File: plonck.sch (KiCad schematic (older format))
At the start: 127 parts, among them J1 Battery_connector, J2 SWD, Q1 Q_PMOS_GSD, SW1 SW_Push, U1 SRV05-4, U2 TP4054-42-SOT25-R, U3 XC6206PxxxMR-Regulator_Linear, U4 nRF52840_holyiot_18010, q1 USB4085-GF-A_REVA

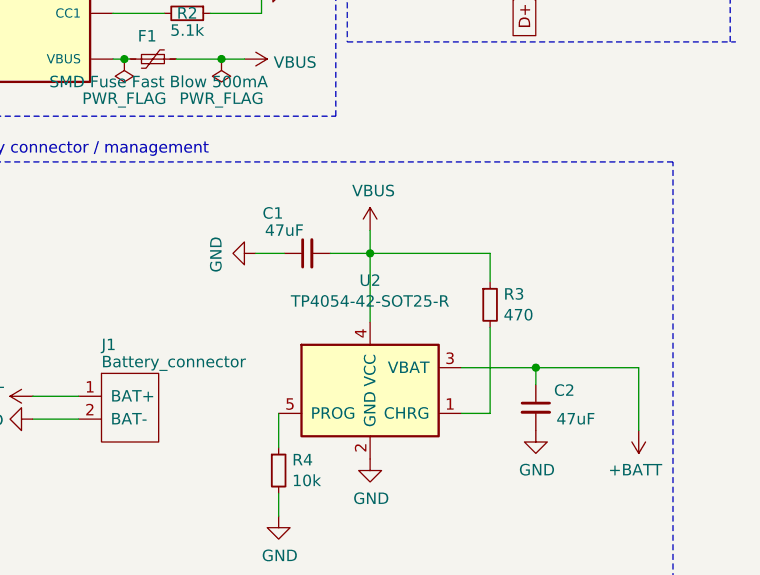
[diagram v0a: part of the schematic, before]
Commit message: added charge status led
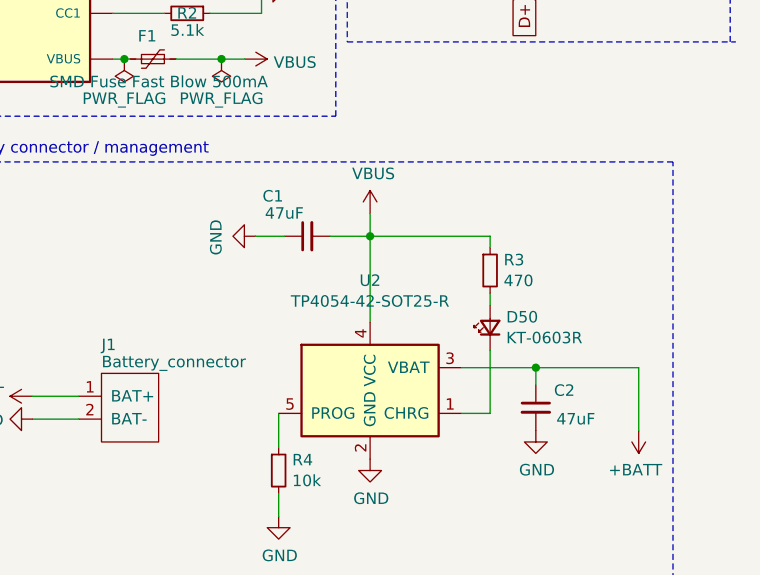
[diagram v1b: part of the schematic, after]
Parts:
- added D50: KT-0603R, LED_SMD:LED_0603_1608Metric, symbol Device:LED_Small
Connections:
- net at R3.2: now also D50.2 (A); no longer U2.1 (CHRG)
- new net: D50.1 (K), U2.1 (CHRG)
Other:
- moved on the sheet: C1, R3
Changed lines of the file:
@@
 L Device:C_Small C1
 U 1 1 60625507
-P 8775 3075
-F 0 "C1" V 8950 3225 50  0000 C CNN
-F 1 "47uF" V 8875 3175 50  0000 C CNN
-F 2 "Capacitor_SMD:C_1206_3216Metric" H 8775 3075 50  0001 C CNN
-F 3 "~" H 8775 3075 50  0001 C CNN
-F 4 "C96123" H 8775 3075 50  0001 C CNN "LCSC"
-	1    8775 3075
+P 8775 3000
+F 0 "C1" V 8950 3150 50  0000 C CNN
+F 1 "47uF" V 8875 3100 50  0000 C CNN
+F 2 "Capacitor_SMD:C_1206_3216Metric" H 8775 3000 50  0001 C CNN
+F 3 "~" H 8775 3000 50  0001 C CNN
+F 4 "C96123" H 8775 3000 50  0001 C CNN "LCSC"
+	1    8775 3000
 	0    -1   -1   0
 $EndComp
 Wire Wire Line
-	9050 2975 9050 3075
-Wire Wire Line
-	8875 3075 9050 3075
-Wire Wire Line
-	8550 3075 8675 3075
+	9050 2900 9050 3000
+Wire Wire Line
+	8875 3000 9050 3000
+Wire Wire Line
+	8550 3000 8675 3000
 $Comp
 L power:GND #PWR07
 U 1 1 6063374E
-P 8550 3075
-F 0 "#PWR07" H 8550 2825 50  0001 C CNN
-F 1 "GND" H 8555 2902 50  0000 C CNN
-F 2 "" H 8550 3075 50  0001 C CNN
-F 3 "" H 8550 3075 50  0001 C CNN
-	1    8550 3075
+P 8550 3000
+F 0 "#PWR07" H 8550 2750 50  0001 C CNN
+F 1 "GND" H 8555 2827 50  0000 C CNN
+F 2 "" H 8550 3000 50  0001 C CNN
+F 3 "" H 8550 3000 50  0001 C CNN
+	1    8550 3000
 	0    1    1    0
 $EndComp
-Connection ~ 9050 3075
-Wire Wire Line
-	9050 3075 9050 3375
-Wire Wire Line
-	9050 3075 9575 3075
-Wire Wire Line
-	9575 3075 9575 3200
-Wire Wire Line
-	9575 3775 9575 3400
+Connection ~ 9050 3000
+Wire Wire Line
+	9050 3000 9050 3375
+Wire Wire Line
+	9050 3000 9575 3000
+Wire Wire Line
+	9575 3000 9575 3050
+Wire Wire Line
+	9575 3775 9575 3500
 Wire Wire Line
 	9575 3775 9450 3775
@@
 L power:VBUS #PWR06
 U 1 1 607C3C76
-P 9050 2975
-F 0 "#PWR06" H 9050 2825 50  0001 C CNN
-F 1 "VBUS" H 9065 3148 50  0000 C CNN
-F 2 "" H 9050 2975 50  0001 C CNN
-F 3 "" H 9050 2975 50  0001 C CNN
-	1    9050 2975
+P 9050 2900
+F 0 "#PWR06" H 9050 2750 50  0001 C CNN
+F 1 "VBUS" H 9065 3073 50  0000 C CNN
+F 2 "" H 9050 2900 50  0001 C CNN
+F 3 "" H 9050 2900 50  0001 C CNN
+	1    9050 2900
 	1    0    0    -1
 $EndComp
@@
 L Device:R_Small R3
 U 1 1 6063443F
-P 9575 3300
-F 0 "R3" H 9634 3346 50  0000 L CNN
-F 1 "470" H 9634 3255 50  0000 L CNN
-F 2 "Resistor_SMD:R_0603_1608Metric" H 9575 3300 50  0001 C CNN
-F 3 "~" H 9575 3300 50  0001 C CNN
-F 4 "RMCF0603JT470RTR-ND" H 9575 3300 50  0001 C CNN "Digikey"
-F 5 "C23179" H 9575 3300 50  0001 C CNN "LCSC"
-	1    9575 3300
+P 9575 3150
+F 0 "R3" H 9634 3196 50  0000 L CNN
+F 1 "470" H 9634 3105 50  0000 L CNN
+F 2 "Resistor_SMD:R_0603_1608Metric" H 9575 3150 50  0001 C CNN
+F 3 "~" H 9575 3150 50  0001 C CNN
+F 4 "RMCF0603JT470RTR-ND" H 9575 3150 50  0001 C CNN "Digikey"
+F 5 "C23179" H 9575 3150 50  0001 C CNN "LCSC"
+	1    9575 3150
 	1    0    0    -1
 $EndComp
@@
 Wire Notes Line
 	2375 6550 3325 6550
+$Comp
+L Device:LED_Small D50
+U 1 1 60BDAFE9
+P 9575 3400
+F 0 "D50" V 9621 3330 50  0000 R CNN
+F 1 "KT-0603R" V 9530 3330 50  0000 R CNN
+F 2 "LED_SMD:LED_0603_1608Metric" V 9575 3400 50  0001 C CNN
+F 3 "https://datasheet.lcsc.com/szlcsc/Hubei-KENTO-Elec-KT-0603R_C2286.pdf" V 9575 3400 50  0001 C CNN
+F 4 "C2286" H 9575 3400 50  0001 C CNN "LCSC"
+	1    9575 3400
+	0    -1   -1   0
+$EndComp
+Wire Wire Line
+	9575 3300 9575 3250
 $EndSCHEMATC

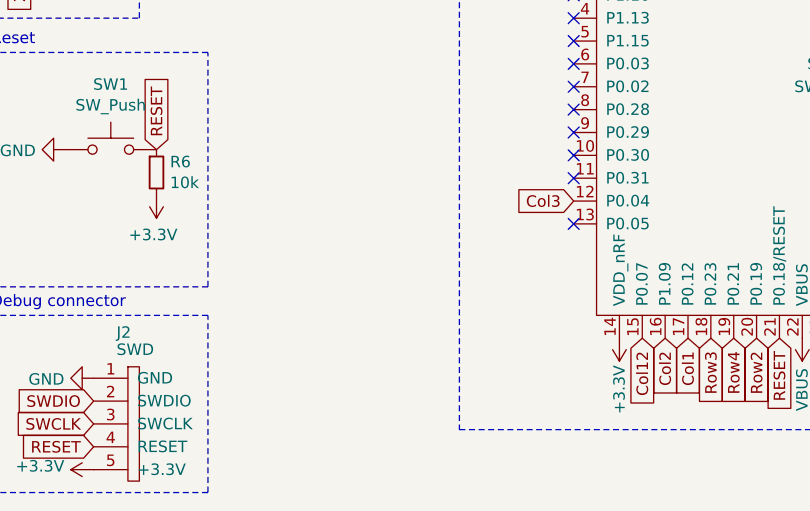
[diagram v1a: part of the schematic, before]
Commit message: added vsense circuitry
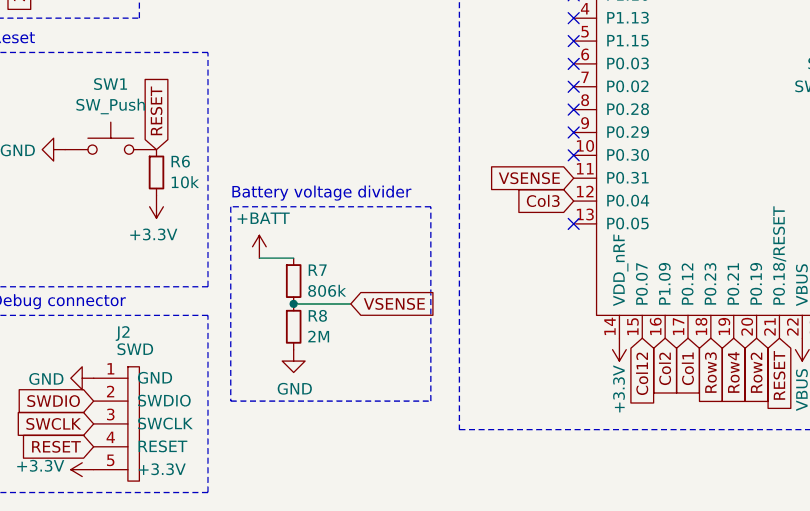
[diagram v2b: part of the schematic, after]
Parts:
- added R7: 806k, Resistor_SMD:R_0603_1608Metric, symbol Device:R_Small
- added R8: 2M, Resistor_SMD:R_0603_1608Metric, symbol Device:R_Small
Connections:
- net +BATT: now also R7.1
- net GND: now also R8.2
- net VSENSE: now reaches U4.11 (P0.31)
- net VSENSE: now also R7.2, R8.1
- no-connect marks 15 -> 14
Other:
- note added: "Battery voltage divider"
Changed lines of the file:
@@
 Col3
 NoConn ~ 4925 6275
-NoConn ~ 4925 6075
 NoConn ~ 4925 5975
 NoConn ~ 4925 5875
@@
 Wire Wire Line
 	9575 3300 9575 3250
+$Comp
+L power:+BATT #PWR0101
+U 1 1 60C1F4E5
+P 3550 6425
+F 0 "#PWR0101" H 3550 6275 50  0001 C CNN
+F 1 "+BATT" H 3565 6598 50  0000 C CNN
+F 2 "" H 3550 6425 50  0001 C CNN
+F 3 "" H 3550 6425 50  0001 C CNN
+	1    3550 6425
+	1    0    0    -1
+$EndComp
+$Comp
+L Device:R_Small R7
+U 1 1 60C2226C
+P 3700 6525
+F 0 "R7" H 3759 6571 50  0000 L CNN
+F 1 "806k" H 3759 6480 50  0000 L CNN
+F 2 "Resistor_SMD:R_0603_1608Metric" H 3700 6525 50  0001 C CNN
+F 3 "~" H 3700 6525 50  0001 C CNN
+	1    3700 6525
+	1    0    0    -1
+$EndComp
+$Comp
+L Device:R_Small R8
+U 1 1 60C23717
+P 3700 6725
+F 0 "R8" H 3759 6771 50  0000 L CNN
+F 1 "2M" H 3759 6680 50  0000 L CNN
+F 2 "Resistor_SMD:R_0603_1608Metric" H 3700 6725 50  0001 C CNN
+F 3 "~" H 3700 6725 50  0001 C CNN
+	1    3700 6725
+	1    0    0    -1
+$EndComp
+$Comp
+L power:GND #PWR0102
+U 1 1 60C25DD1
+P 3700 6825
+F 0 "#PWR0102" H 3700 6575 50  0001 C CNN
+F 1 "GND" H 3705 6652 50  0000 C CNN
+F 2 "" H 3700 6825 50  0001 C CNN
+F 3 "" H 3700 6825 50  0001 C CNN
+	1    3700 6825
+	1    0    0    -1
+$EndComp
+Wire Wire Line
+	3550 6425 3700 6425
+Wire Wire Line
+	3700 6625 3950 6625
+Connection ~ 3700 6625
+Text GLabel 3950 6625 2    50   Input ~ 0
+VSENSE
+Wire Notes Line
+	3425 6200 3425 7050
+Wire Notes Line
+	3425 7050 4300 7050
+Wire Notes Line
+	4300 7050 4300 6200
+Wire Notes Line
+	4300 6200 3425 6200
+Text Notes 3425 6175 0    50   ~ 0
+Battery voltage divider
+Text GLabel 4925 6075 0    50   Input ~ 0
+VSENSE
 $EndSCHEMATC

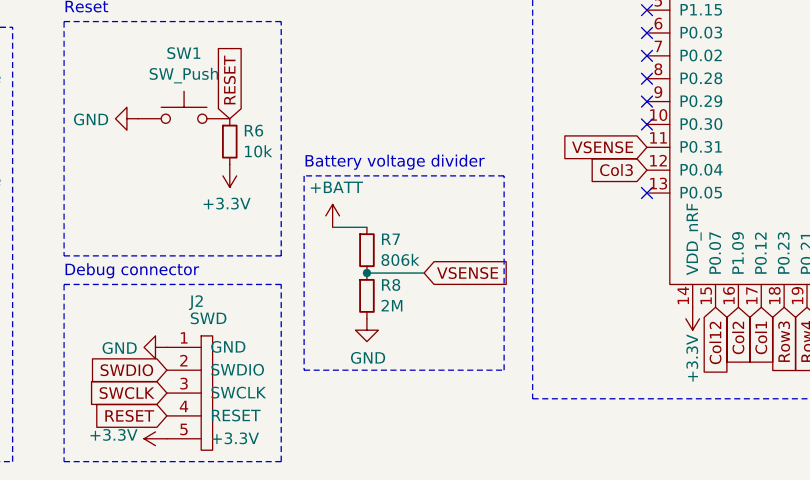
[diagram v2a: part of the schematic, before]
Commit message: updated resistor values in battery voltage divider
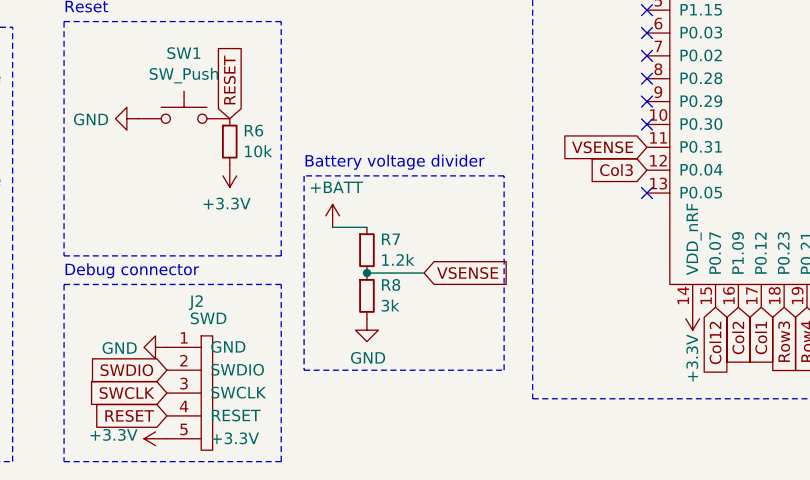
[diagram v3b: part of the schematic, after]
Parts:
- R7: value 806k -> 1.2k; LCSC (none) -> C22765
- R8: value 2M -> 3k; LCSC (none) -> C17661
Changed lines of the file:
@@
 P 3700 6525
 F 0 "R7" H 3759 6571 50  0000 L CNN
-F 1 "806k" H 3759 6480 50  0000 L CNN
+F 1 "1.2k" H 3759 6480 50  0000 L CNN
 F 2 "Resistor_SMD:R_0603_1608Metric" H 3700 6525 50  0001 C CNN
-F 3 "~" H 3700 6525 50  0001 C CNN
+F 3 "https://datasheet.lcsc.com/lcsc/1811021221_UNI-ROYAL-Uniroyal-Elec-0603WAF1201T5E_C22765.pdf" H 3700 6525 50  0001 C CNN
+F 4 "C22765" H 3700 6525 50  0001 C CNN "LCSC"
 	1    3700 6525
 	1    0    0    -1
@@
 P 3700 6725
 F 0 "R8" H 3759 6771 50  0000 L CNN
-F 1 "2M" H 3759 6680 50  0000 L CNN
+F 1 "3k" H 3759 6680 50  0000 L CNN
 F 2 "Resistor_SMD:R_0603_1608Metric" H 3700 6725 50  0001 C CNN
-F 3 "~" H 3700 6725 50  0001 C CNN
+F 3 "https://datasheet.lcsc.com/lcsc/1811131122_UNI-ROYAL-Uniroyal-Elec-0805W8F3001T5E_C17661.pdf" H 3700 6725 50  0001 C CNN
+F 4 "C17661" H 3700 6725 50  0001 C CNN "LCSC"
 	1    3700 6725
 	1    0    0    -1

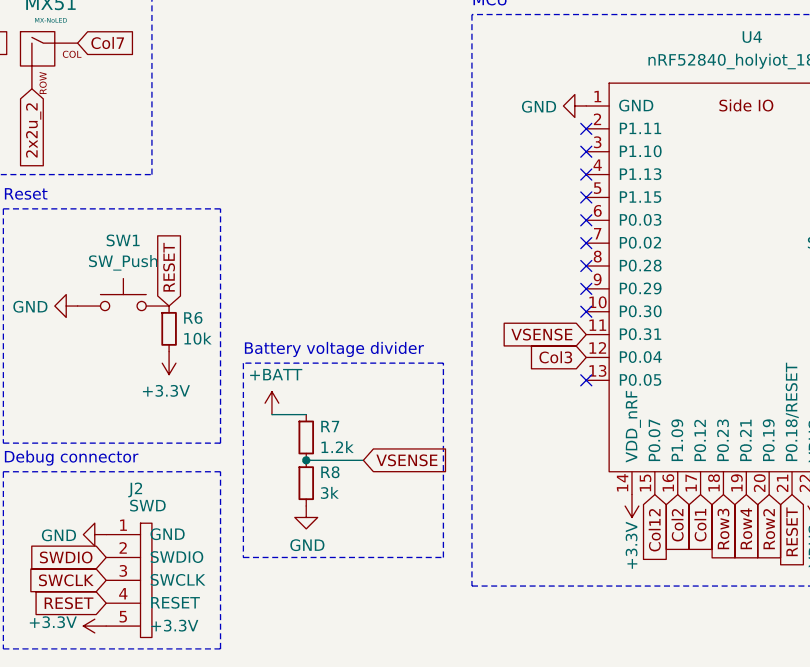
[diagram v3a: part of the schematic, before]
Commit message: added bootloader status led
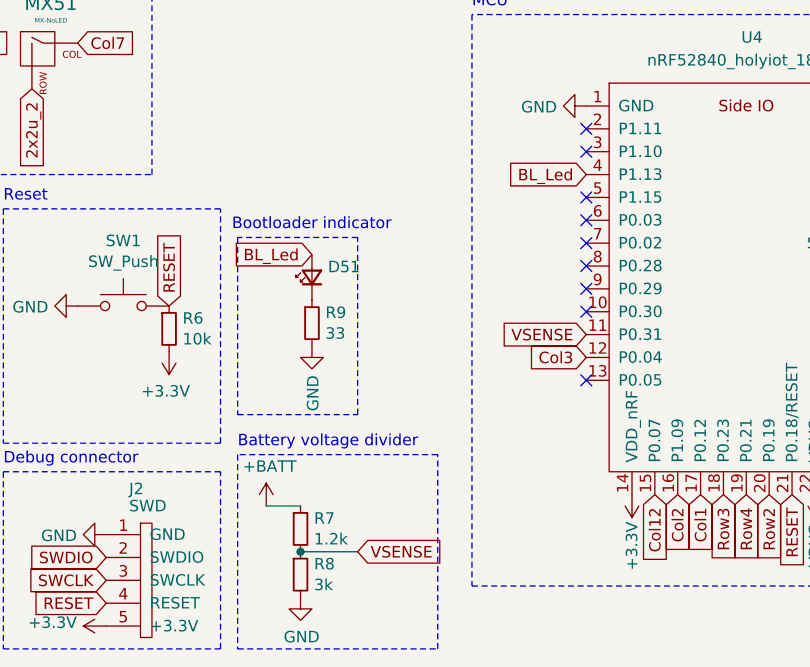
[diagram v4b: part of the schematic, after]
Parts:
- added D51: 19-217/BHC-ZL1M2RY/3T, LED_SMD:LED_0603_1608Metric, symbol Device:LED_Small
- added R9: 33, Resistor_SMD:R_0603_1608Metric, symbol Device:R_Small
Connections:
- net GND: now also R9.2
- net BL_Led: now reaches U4.4 (P1.13)
- net BL_Led: now also D51.2 (A)
- new net: D51.1 (K), R9.1
- no-connect marks 14 -> 13
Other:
- note added: "Bootloader indicator"
- moved on the sheet: R7, R8
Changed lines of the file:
@@
 NoConn ~ 4925 5575
 NoConn ~ 4925 5475
-NoConn ~ 4925 5375
 NoConn ~ 4925 5275
 NoConn ~ 4925 5175
@@
 L power:+BATT #PWR0101
 U 1 1 60C1F4E5
-P 3550 6425
-F 0 "#PWR0101" H 3550 6275 50  0001 C CNN
-F 1 "+BATT" H 3565 6598 50  0000 C CNN
-F 2 "" H 3550 6425 50  0001 C CNN
-F 3 "" H 3550 6425 50  0001 C CNN
-	1    3550 6425
+P 3525 6825
+F 0 "#PWR0101" H 3525 6675 50  0001 C CNN
+F 1 "+BATT" H 3540 6998 50  0000 C CNN
+F 2 "" H 3525 6825 50  0001 C CNN
+F 3 "" H 3525 6825 50  0001 C CNN
+	1    3525 6825
 	1    0    0    -1
 $EndComp
@@
 L Device:R_Small R7
 U 1 1 60C2226C
-P 3700 6525
-F 0 "R7" H 3759 6571 50  0000 L CNN
-F 1 "1.2k" H 3759 6480 50  0000 L CNN
-F 2 "Resistor_SMD:R_0603_1608Metric" H 3700 6525 50  0001 C CNN
-F 3 "https://datasheet.lcsc.com/lcsc/1811021221_UNI-ROYAL-Uniroyal-Elec-0603WAF1201T5E_C22765.pdf" H 3700 6525 50  0001 C CNN
-F 4 "C22765" H 3700 6525 50  0001 C CNN "LCSC"
-	1    3700 6525
+P 3675 6925
+F 0 "R7" H 3734 6971 50  0000 L CNN
+F 1 "1.2k" H 3734 6880 50  0000 L CNN
+F 2 "Resistor_SMD:R_0603_1608Metric" H 3675 6925 50  0001 C CNN
+F 3 "https://datasheet.lcsc.com/lcsc/1811021221_UNI-ROYAL-Uniroyal-Elec-0603WAF1201T5E_C22765.pdf" H 3675 6925 50  0001 C CNN
+F 4 "C22765" H 3675 6925 50  0001 C CNN "LCSC"
+	1    3675 6925
 	1    0    0    -1
 $EndComp
@@
 L Device:R_Small R8
 U 1 1 60C23717
-P 3700 6725
-F 0 "R8" H 3759 6771 50  0000 L CNN
-F 1 "3k" H 3759 6680 50  0000 L CNN
-F 2 "Resistor_SMD:R_0603_1608Metric" H 3700 6725 50  0001 C CNN
-F 3 "https://datasheet.lcsc.com/lcsc/1811131122_UNI-ROYAL-Uniroyal-Elec-0805W8F3001T5E_C17661.pdf" H 3700 6725 50  0001 C CNN
-F 4 "C17661" H 3700 6725 50  0001 C CNN "LCSC"
-	1    3700 6725
+P 3675 7125
+F 0 "R8" H 3734 7171 50  0000 L CNN
+F 1 "3k" H 3734 7080 50  0000 L CNN
+F 2 "Resistor_SMD:R_0603_1608Metric" H 3675 7125 50  0001 C CNN
+F 3 "https://datasheet.lcsc.com/lcsc/1811131122_UNI-ROYAL-Uniroyal-Elec-0805W8F3001T5E_C17661.pdf" H 3675 7125 50  0001 C CNN
+F 4 "C17661" H 3675 7125 50  0001 C CNN "LCSC"
+	1    3675 7125
 	1    0    0    -1
 $EndComp
@@
 L power:GND #PWR0102
 U 1 1 60C25DD1
-P 3700 6825
-F 0 "#PWR0102" H 3700 6575 50  0001 C CNN
-F 1 "GND" H 3705 6652 50  0000 C CNN
-F 2 "" H 3700 6825 50  0001 C CNN
-F 3 "" H 3700 6825 50  0001 C CNN
-	1    3700 6825
-	1    0    0    -1
-$EndComp
-Wire Wire Line
-	3550 6425 3700 6425
-Wire Wire Line
-	3700 6625 3950 6625
-Connection ~ 3700 6625
-Text GLabel 3950 6625 2    50   Input ~ 0
+P 3675 7225
+F 0 "#PWR0102" H 3675 6975 50  0001 C CNN
+F 1 "GND" H 3680 7052 50  0000 C CNN
+F 2 "" H 3675 7225 50  0001 C CNN
+F 3 "" H 3675 7225 50  0001 C CNN
+	1    3675 7225
+	1    0    0    -1
+$EndComp
+Wire Wire Line
+	3525 6825 3675 6825
+Wire Wire Line
+	3675 7025 3925 7025
+Connection ~ 3675 7025
+Text GLabel 3925 7025 2    50   Input ~ 0
 VSENSE
 Wire Notes Line
-	3425 6200 3425 7050
-Wire Notes Line
-	3425 7050 4300 7050
-Wire Notes Line
-	4300 7050 4300 6200
-Wire Notes Line
-	4300 6200 3425 6200
-Text Notes 3425 6175 0    50   ~ 0
+	3400 6600 3400 7450
+Wire Notes Line
+	3400 7450 4275 7450
+Wire Notes Line
+	4275 7450 4275 6600
+Wire Notes Line
+	4275 6600 3400 6600
+Text Notes 3400 6575 0    50   ~ 0
 Battery voltage divider
 Text GLabel 4925 6075 0    50   Input ~ 0
 VSENSE
+Text GLabel 3725 5725 0    50   Input ~ 0
+BL_Led
+$Comp
+L Device:LED_Small D51
+U 1 1 60BA6345
+P 3725 5825
+F 0 "D51" V 3771 5755 50  0000 R CNN
+F 1 "19-217/BHC-ZL1M2RY/3T" V 3680 5755 50  0001 R CNN
+F 2 "LED_SMD:LED_0603_1608Metric" V 3725 5825 50  0001 C CNN
+F 3 "https://datasheet.lcsc.com/lcsc/1811101510_Everlight-Elec-19-217-BHC-ZL1M2RY-3T_C72041.pdf" V 3725 5825 50  0001 C CNN
+F 4 "C72041" H 3725 5825 50  0001 C CNN "LCSC"
+	1    3725 5825
+	0    -1   -1   0
+$EndComp
+$Comp
+L power:GND #PWR035
+U 1 1 60BA897F
+P 3725 6125
+F 0 "#PWR035" H 3725 5875 50  0001 C CNN
+F 1 "GND" V 3730 5997 50  0000 R CNN
+F 2 "" H 3725 6125 50  0001 C CNN
+F 3 "" H 3725 6125 50  0001 C CNN
+	1    3725 6125
+	1    0    0    -1
+$EndComp
+$Comp
+L Device:R_Small R9
+U 1 1 60BAB72D
+P 3725 6025
+F 0 "R9" H 3784 6071 50  0000 L CNN
+F 1 "33" H 3784 5980 50  0000 L CNN
+F 2 "Resistor_SMD:R_0603_1608Metric" H 3725 6025 50  0001 C CNN
+F 3 "https://datasheet.lcsc.com/szlcsc/Uniroyal-Elec-0603WAF330JT5E_C23140.pdf" H 3725 6025 50  0001 C CNN
+F 4 "C23140" H 3725 6025 50  0001 C CNN "LCSC"
+	1    3725 6025
+	1    0    0    -1
+$EndComp
+Wire Notes Line
+	3400 5650 3400 6425
+Wire Notes Line
+	3400 6425 3925 6425
+Wire Notes Line
+	3925 6425 3925 5650
+Wire Notes Line
+	3925 5650 3400 5650
+Text Notes 3375 5625 0    50   ~ 0
+Bootloader indicator
+Text GLabel 4925 5375 0    50   Input ~ 0
+BL_Led
 $EndSCHEMATC
